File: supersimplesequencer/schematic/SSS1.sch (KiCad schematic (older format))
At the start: 56 parts, among them J1 RESET_IN, J2 CLK_IN, J3 STEP1_OUT, J4 CV1_OUT, J5 CV2_OUT, J6 GATE_OUT, J7 POWER, SW1 CV2_SCALE, U1 40106, U2 4017, U3 NE555, U4 LM324

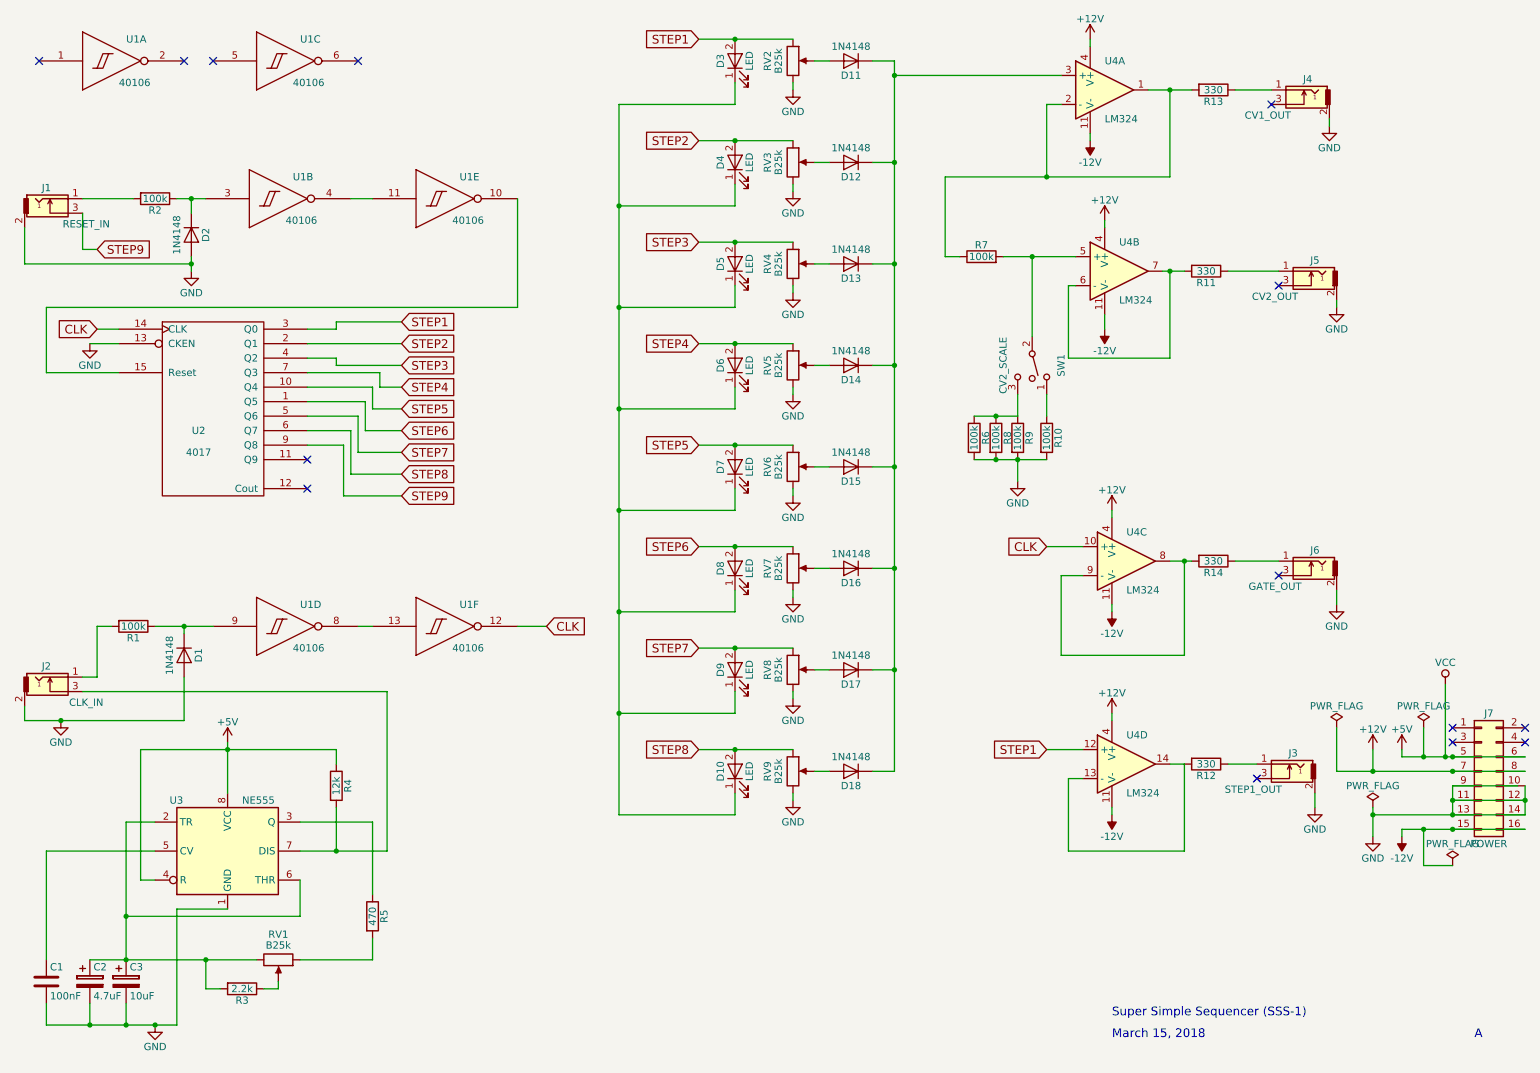
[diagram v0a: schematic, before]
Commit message: Update schematic with new components
Replace annoying ones with hidden power with my copies that
have power. So.
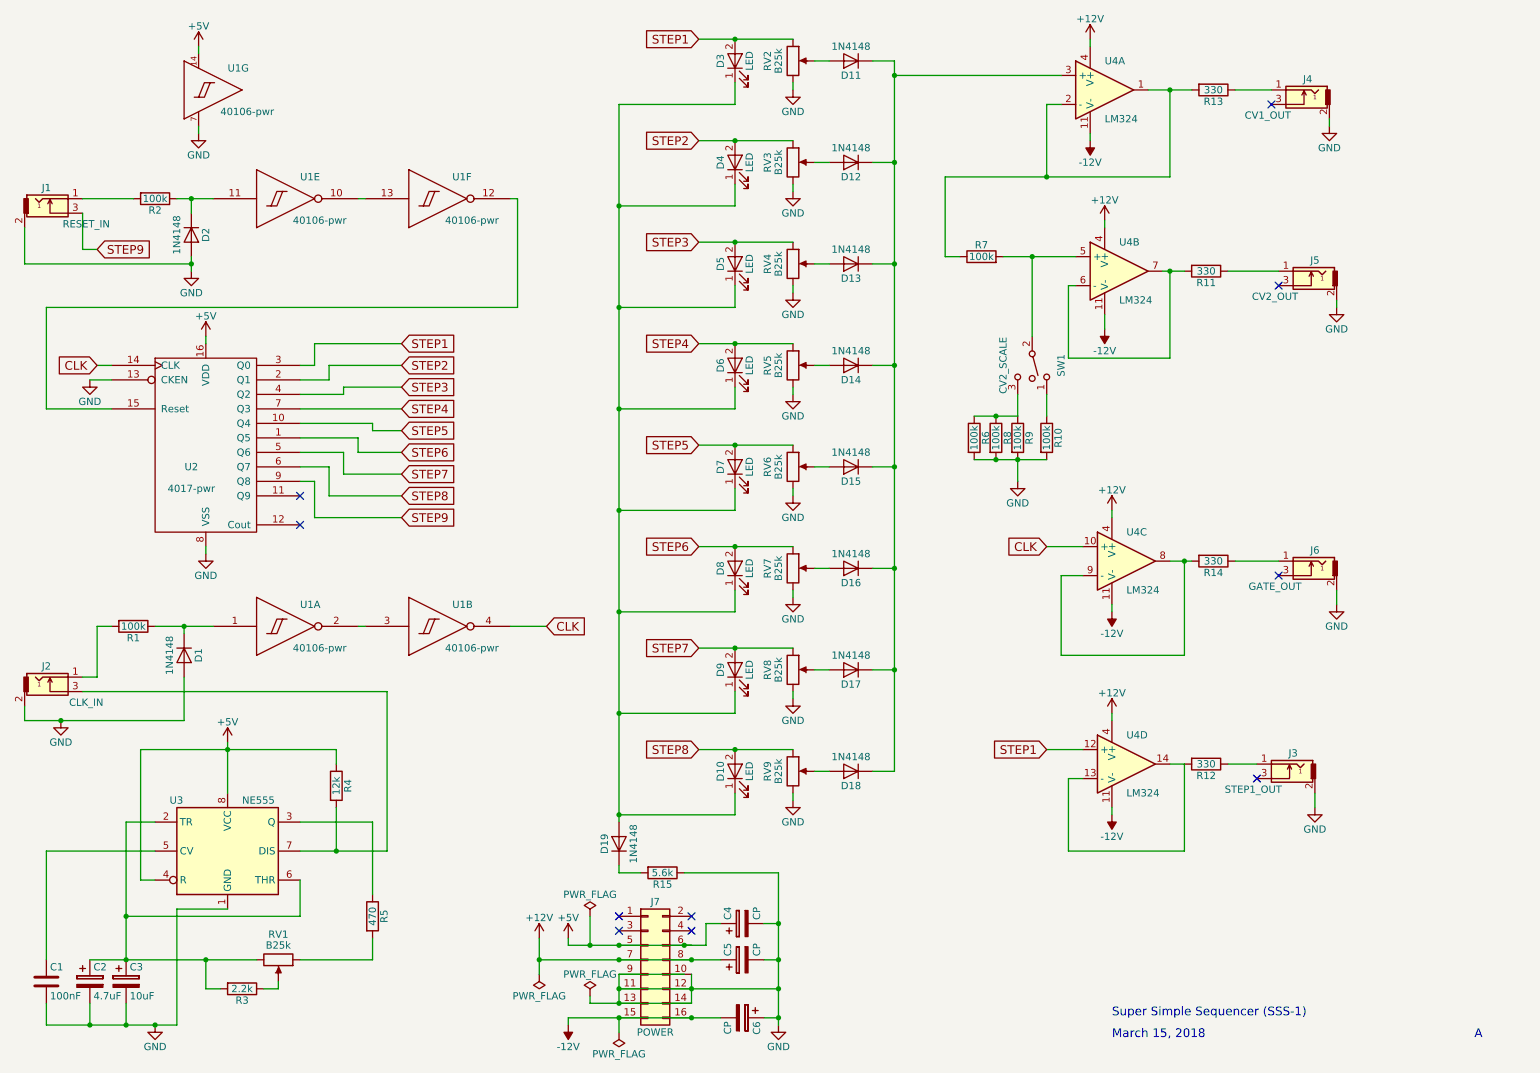
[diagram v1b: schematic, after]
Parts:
- removed U1: 40106, symbol 40106
- removed U2: 4017, symbol 4017
- added C4, C5, C6: CP, symbol CP
- added D19: 1N4148, symbol D
- added R15: 5.6k, symbol R
- added U1: 40106-pwr, symbol 40106-pwr
- added U2: 4017-pwr, symbol 4017-pwr
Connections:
- net +12V: now also C5.1
- net +5V: now also C4.1, U1.14 (VDD), U2.16 (VDD)
- net -12V: now also C6.2
- net CLK: now also U1.4 (Out), U2.14 (CLK)
- net GND: now also C4.2, C5.2, C6.1, R15.1, U1.7 (VSS), U2.13 (CKEN), U2.8 (VSS)
- net STEP1: now also U2.3 (Q0)
- net STEP2: now also U2.2 (Q1)
- net STEP3: now also U2.4 (Q2)
- net STEP4: now also U2.7 (Q3)
- net STEP5: now also U2.10 (Q4)
- net STEP6: now also U2.1 (Q5)
- net STEP7: now also U2.5 (Q6)
- net STEP8: now also U2.6 (Q7)
- net STEP9: now also U2.9 (Q8)
- net at D1.1 (K), R1.1: now also U1.1 (In)
- net at D2.1 (K), R2.1: now also U1.11 (In)
- net at D10.1 (K), D3.1 (K), D4.1 (K)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: now also D19.2 (A)
- new net: U1.2 (Out), U1.3 (In)
- new net: U1.10 (Out), U1.13 (In)
- new net: U1.12 (Out), U2.15 (Reset)
- new net: D19.1 (K), R15.2
- no-connect marks 14 -> 10
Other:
- moved on the sheet: J7

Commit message: Add first attempt towards PCB layout of SSS-1
Well, it's a start...

Inspiration and help from e.g.:
http://www.xess.com/blog/my-first-kicad-board/
and obviously Contextual Electronics' YouTube tutorials, mainly
various bits of the "Getting To Blinky" series.
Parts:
- C1: footprint (none) -> Capacitors_THT:C_Rect_L9.0mm_W3.3mm_P7.50mm_MKT
- C2, C3, C4, C5, C6: footprint (none) -> Capacitors_THT:CP_Radial_D10.0mm_P5.00mm
- D1, D11, D12, D13, D14, D15, D16, D17, D18, D19, D2: footprint (none) -> Diodes_THT:D_A-405_P7.62mm_Horizontal
- D10, D3, D4, D5, D6, D7, D8, D9: footprint (none) -> LEDs:LED_D3.0mm
- J1, J2, J3, J4, J5, J6, SW1: footprint (none) -> Socket_Strips:Socket_Strip_Straight_1x03_Pitch2.54mm
- J7: footprint (none) -> Pin_Headers:Pin_Header_Straight_2x08_Pitch2.54mm
- R1, R10, R11, R12, R13, R14, R15, R2, R3, R4, R5, R6, R7, R8, R9: footprint (none) -> Resistors_THT:R_Axial_DIN0207_L6.3mm_D2.5mm_P7.62mm_Horizontal
- RV1, RV2, RV3, RV4, RV5, RV6, RV7, RV8, RV9: footprint (none) -> Potentiometers:Potentiometer_Alps_RK09Y_Vertical
- U1, U4: footprint (none) -> Housings_DIP:DIP-14_W7.62mm_Socket_LongPads
- U2: footprint (none) -> Housings_DIP:DIP-16_W7.62mm_Socket_LongPads
- U3: footprint (none) -> Housings_DIP:DIP-8_W7.62mm_Socket_LongPads

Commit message: Update SSS-1 to beyond prototype
Adding features after using the stripboard prototype a bit, like e.g.:
- Searate output for all steps.
- Using 12V logic (will probably use the small connector for all PCBs).
- Switch for hold/run.
- Switch for step.
- Switch for reset.

The last three untested at this time.
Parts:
- removed C4: CP, Capacitors_THT:CP_Radial_D10.0mm_P5.00mm, symbol CP
- removed D11, D12, D13, D14, D15, D16, D17, D18: 1N4148, Diodes_THT:D_A-405_P7.62mm_Horizontal, symbol D
- removed J3: STEP1_OUT, Socket_Strips:Socket_Strip_Straight_1x03_Pitch2.54mm, symbol Audio-Jack-2_Switch
- removed J4: CV1_OUT, Socket_Strips:Socket_Strip_Straight_1x03_Pitch2.54mm, symbol Audio-Jack-2_Switch
- removed J5: CV2_OUT, Socket_Strips:Socket_Strip_Straight_1x03_Pitch2.54mm, symbol Audio-Jack-2_Switch
- removed J6: GATE_OUT, Socket_Strips:Socket_Strip_Straight_1x03_Pitch2.54mm, symbol Audio-Jack-2_Switch
- removed R13: 330, Resistors_THT:R_Axial_DIN0207_L6.3mm_D2.5mm_P7.62mm_Horizontal, symbol R
- removed R6: 100k, Resistors_THT:R_Axial_DIN0207_L6.3mm_D2.5mm_P7.62mm_Horizontal, symbol R
- removed U4: LM324, Housings_DIP:DIP-14_W7.62mm_Socket_LongPads, symbol LM324
- added C1, C10, C11, C12, C13, C14, C15, C16, C17, C18, C5, C6, C9: 100nF, Capacitors_THT:C_Rect_L7.2mm_W3.5mm_P5.00mm_FKS2_FKP2_MKS2_MKP2, symbol C
- added D3, D4: 1N4148, Diodes_THT:D_A-405_P7.62mm_Horizontal, symbol D
- added D5: LED, LEDs:LED_D3.0mm, symbol LED
- added D6, D7: 1N4001, Diodes_THT:D_DO-41_SOD81_Horizontal_RM10, symbol 1N4001
- added J4: OUTPUTS, Pin_Headers:Pin_Header_Straight_1x12_Pitch2.54mm, symbol Conn_01x12
- added R1, R2, R3, R4, R7: 10k, Resistors_THT:R_Axial_DIN0207_L6.3mm_D2.5mm_P7.62mm_Horizontal, symbol R
- added R14, R36, R37, R38, R39, R40, R41, R42: 270, Resistors_THT:R_Axial_DIN0207_L6.3mm_D2.5mm_P7.62mm_Horizontal, symbol R
- added R15: 1k, Resistors_THT:R_Axial_DIN0207_L6.3mm_D2.5mm_P7.62mm_Horizontal, symbol R
- added R20: 2.7M, Resistors_THT:R_Axial_DIN0207_L6.3mm_D2.5mm_P7.62mm_Horizontal, symbol R
- added R21, R22, R23, R24, R25, R26, R27, R28, R30: 100k, Resistors_THT:R_Axial_DIN0207_L6.3mm_D2.5mm_P7.62mm_Horizontal, symbol R
- added R31: 82k, Resistors_THT:R_Axial_DIN0207_L6.3mm_D2.5mm_P7.62mm_Horizontal, symbol R
- added R? (x10): 180, symbol R
- added RV11, RV12, RV13: 20k, Potentiometers:Potentiometer_Trimmer_Vishay_T73XX_Vertical, symbol POT_TRIM
- added RV2: 100k, Potentiometers:Potentiometer_Trimmer_Vishay_T73XX_Vertical, symbol POT_TRIM
- added SW1: RESET, Pin_Headers:Pin_Header_Straight_2x01_Pitch2.54mm, symbol SW_Push
- added SW2: STEP, Pin_Headers:Pin_Header_Straight_2x01_Pitch2.54mm, symbol SW_Push
- added SW3: HOLD_RUN, Pin_Headers:Pin_Header_Straight_1x03_Pitch2.54mm, symbol SW_SPDT
- added unit 5 of U1
- added unit 3 of U1
- added U4: 4011, Housings_DIP:DIP-14_W7.62mm_LongPads, symbol 4011
- added U5, U6, U7: TL074, Housings_DIP:DIP-14_W7.62mm_LongPads, symbol TL074
- C2: renamed from C1; footprint Capacitors_THT:C_Rect_L9.0mm_W3.3mm_P7.50mm_MKT -> Capacitors_THT:C_Rect_L7.2mm_W3.5mm_P5.00mm_FKS2_FKP2_MKS2_MKP2
- C3: renamed from C2; footprint Capacitors_THT:CP_Radial_D10.0mm_P5.00mm -> Capacitors_THT:CP_Radial_D5.0mm_P2.00mm
- C4: renamed from C3; footprint Capacitors_THT:CP_Radial_D10.0mm_P5.00mm -> Capacitors_THT:CP_Radial_D5.0mm_P2.00mm
- C7: renamed from C5; value CP -> 10uF; footprint Capacitors_THT:CP_Radial_D10.0mm_P5.00mm -> Capacitors_THT:CP_Radial_D5.0mm_P2.00mm
- C8: renamed from C6; value CP -> 10uF; footprint Capacitors_THT:CP_Radial_D10.0mm_P5.00mm -> Capacitors_THT:CP_Radial_D5.0mm_P2.00mm
- J3: renamed from J7; footprint Pin_Headers:Pin_Header_Straight_2x08_Pitch2.54mm -> Pin_Headers:Pin_Header_Straight_2x05_Pitch2.54mm; symbol Conn_02x08_Odd_Even -> Conn_02x05_Odd_Even
- R18: renamed from R14; value 330 -> 100
- R29: renamed from R7; value 100k -> 270k
- R32: renamed from R10; value 100k -> 82k
- R33: renamed from R9; value 100k -> 22k
- R34: renamed from R11; value 330 -> 100
- R35: renamed from R12; value 330 -> 270
- R8: value 100k -> 10k
- renumbered D5 to D10, D6 to D11, D7 to D12, D8 to D13, D9 to D14, D10 to D15, D19 to D16, D3 to D8, D4 to D9, R5 to R10, R4 to R11, R15 to R19, R1 to R5, R2 to R6, R3 to R9, RV9 to RV10, RV2 to RV3, RV3 to RV4, RV4 to RV5, RV5 to RV6, RV6 to RV7, RV7 to RV8, RV8 to RV9, SW1 to SW4
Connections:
- net +12V: now also J3.10 (Pin_10), J3.9 (Pin_9), R11.1, U1.14 (VDD), U2.16 (VDD), U3.4 (R), U3.8 (VCC), C11.1, C13.1, C15.1, C16.1, C17.1, C18.1, C9.1, D6.1 (K), R1.1, R3.1, R4.1, U4.14 (VDD), U4.14 (VDD), U4.14 (VDD), U4.14 (VDD), U5.4 (V+), U5.4 (V+), U5.4 (V+), U5.4 (V+), U6.4 (V+), U6.4 (V+), U6.4 (V+), U6.4 (V+), U7.4 (V+), U7.4 (V+), U7.4 (V+), U7.4 (V+); no longer J3.7 (Pin_7), J3.8 (Pin_8)
- net -12V: now also J3.1 (Pin_1), J3.2 (Pin_2), C10.2, C12.2, C14.2, D7.2 (A), RV2.1, U5.11 (V-), U5.11 (V-), U5.11 (V-), U5.11 (V-), U6.11 (V-), U6.11 (V-), U6.11 (V-), U6.11 (V-), U7.11 (V-), U7.11 (V-), U7.11 (V-), U7.11 (V-); no longer J3.15 (Pin_15), J3.16 (Pin_16)
- net GND: now also J3.3 (Pin_3), J3.4 (Pin_4), J3.5 (Pin_5), J3.6 (Pin_6), J3.7 (Pin_7), J3.8 (Pin_8), C1.2, C10.1, C11.2, C12.1, C13.2, C14.1, C15.2, C16.2, C17.2, C18.2, C5.2, C6.2, C9.2, D6.2 (A), D7.1 (K), J4.12 (Pin_12), R15.2, R?.2, R?.2, R?.2, R?.2, R?.2, R?.2, R?.2, R?.2, R?.2, R?.2, RV2.3, SW1.1, SW2.1, SW3.3 (C), U4.7 (VSS), U4.7 (VSS), U4.7 (VSS), U4.7 (VSS), U5.10 (+), U5.12 (+); no longer J3.10 (Pin_10), J3.11 (Pin_11), J3.12 (Pin_12), J3.13 (Pin_13), J3.14 (Pin_14), J3.9 (Pin_9), R32.2, R33.2, R8.2
- net STEP1: now also U6.3 (+)
- net STEP2: now also U6.5 (+)
- net STEP3: now also U6.10 (+)
- net STEP4: now also U6.12 (+)
- net STEP5: now also U7.3 (+)
- net STEP6: now also U7.5 (+)
- net STEP7: now also U7.10 (+)
- net STEP8: now also U7.12 (+)
- net at J2.3, R11.2, U3.7 (DIS): now also U5.3 (+)
- net at R29.1: now also R30.2, U5.8
- net at R29.2, SW4.2: now also R31.1, U5.13 (-)
- net at R34.2: now also RV11.2, RV11.3, RV12.2, RV12.3, RV13.2, RV13.3, U5.14
- net at R18.2: now also U5.6 (-), U5.7
- net at R35.2: now also U6.1, U6.2 (-)
- net at RV3.2: now also R21.2
- net at D2.1 (K), R6.1: now also U1.9 (In); no longer U1.11 (In)
- net at R33.1, SW4.3: no longer R8.1
- net CV_OUT: now reaches R34.1
- net CV_OUT: now also J4.11 (Pin_11)
- net at RV4.2: now also R22.2
- net at RV5.2: now also R23.2
- net at RV6.2: now also R24.2
- net at RV7.2: now also R25.2
- net at RV8.2: now also R26.2
- net at RV9.2: now also R27.2
- net at RV10.2: now also R28.2
- net at R35.1: now also J4.1 (Pin_1), R?.1
- net GATE_OUT: now reaches R18.1
- net GATE_OUT: now also J4.9 (Pin_9), R?.1
- net at U1.2 (Out): now also U4.1, U4.2; no longer U1.3 (In)
- net at U1.13 (In): now also U1.10 (Out); no longer U1.10 (Out)
- net at U1.12 (Out): now also U4.5; no longer U2.15 (Reset)
- removed net +5V: J3.5 (Pin_5), J3.6 (Pin_6), R11.1, U1.14 (VDD), U2.16 (VDD), U3.4 (R), U3.8 (VCC)
- net CLK: no longer names the net of U2.14 (CLK)
- net CLK: now also D3.1 (K), D4.1 (K), D5.2 (A), U5.5 (+); no longer U1.4 (Out)
- new net: R33.2, RV13.1
- new net: R32.2, RV12.1
- new net: U1.8 (Out), U4.6
- new net: U2.15 (Reset), U4.4
- new net: R20.1, R21.1, R22.1, R23.1, R24.1, R25.1, R26.1, R27.1, R28.1, R30.1, U5.9 (-)
- new net: R31.2, RV11.1
- new net: J4.2 (Pin_2), R36.1, R?.1
- new net: J4.3 (Pin_3), R37.1, R?.1
- new net: J4.4 (Pin_4), R38.1, R?.1
- new net: J4.5 (Pin_5), R39.1, R?.1
- new net: J4.6 (Pin_6), R40.1, R?.1
- new net: J4.7 (Pin_7), R41.1, R?.1
- new net: J4.8 (Pin_8), R42.1, R?.1
- new net: R36.2, U6.6 (-), U6.7
- new net: R37.2, U6.8, U6.9 (-)
- new net: R38.2, U6.13 (-), U6.14
- new net: R39.2, U7.1, U7.2 (-)
- new net: R40.2, U7.6 (-), U7.7
- new net: R41.2, U7.8, U7.9 (-)
- new net: R42.2, U7.13 (-), U7.14
- new net: R20.2, RV2.2
- new net: R14.2, U5.1, U5.2 (-)
- new net: D5.1 (K), R15.1
- new net: R4.2, R8.2, SW3.2 (B)
- new net: C1.1, R2.1, U1.11 (In)
- new net: R1.2, R2.2, SW1.2
- new net: C5.1, R7.1, U1.5 (In)
- new net: D3.2 (A), U1.6 (Out)
- new net: R3.2, R7.2, SW2.2
- new net: C6.1, R8.1, U1.3 (In)
- new net: U1.4 (Out), U4.8
- new net: U4.3, U4.9
- new net: U4.10, U4.12, U4.13
- new net: D4.2 (A), U4.11
- new net CLK_OUT: J4.10 (Pin_10), R14.1, R?.1
- no-connect marks 10 -> 3
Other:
- note added: "August 5, 2018"
- note added: "B"
- note added: "NOTE: Adjust the current limiting resistors for the LEDs (R15 and R19 \nto your liking; a smaller value gives brighter LEDs (too small and \nthey will fry)."
- note added: "NOTE: These trimmers are for adjusting the 1V, 2V, and \n4V output levels. If you don't care about such details, \njust connect a jumper wire instead of the trim pots. \nAlso, adjust R29 if you want higher output in general."
- note added: "NOTE: This trimmer is for adjusting the 0V output \nlevel. If you don't care about such details, just \nskip the trim pot and the adjacent resistor."
- note removed: "A"
- note removed: "March 15, 2018"
- moved on the sheet: C2, C3, C4, C7, C8, D1, D10, D11, D12, D13, D14, D15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

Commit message: Add draft for AS3320 VCF
Still quite unfinished (not even on breadboard yet), but most
stuff theorethically in place. :-)

Also added AS3320 and 3PDT switch to lib.
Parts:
- added J?: BUS, Pin_Headers:Pin_Header_Straight_1x12_Pitch2.54mm, symbol Conn_01x12
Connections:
- net +12V: now also J?.10 (Pin_10)
- net -12V: now also J?.11 (Pin_11)
- net CLK_OUT: now also J4.9 (Pin_9), J?.9 (Pin_9); no longer J4.10 (Pin_10)
- net GATE_OUT: now also J4.10 (Pin_10); no longer J4.9 (Pin_9)
- net GND: now also J?.12 (Pin_12)
- net at J4.1 (Pin_1), R35.1, R?.1: now also J?.1 (Pin_1)
- net at J4.2 (Pin_2), R36.1, R?.1: now also J?.2 (Pin_2)
- net at J4.3 (Pin_3), R37.1, R?.1: now also J?.3 (Pin_3)
- net at J4.4 (Pin_4), R38.1, R?.1: now also J?.4 (Pin_4)
- net at J4.5 (Pin_5), R39.1, R?.1: now also J?.5 (Pin_5)
- net at J4.6 (Pin_6), R40.1, R?.1: now also J?.6 (Pin_6)
- net at J4.7 (Pin_7), R41.1, R?.1: now also J?.7 (Pin_7)
- net at J4.8 (Pin_8), R42.1, R?.1: now also J?.8 (Pin_8)
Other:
- moved on the sheet: J4, R35, R36, R37, R38, R39, R40, R41, R42, R?, U6A, U6B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
